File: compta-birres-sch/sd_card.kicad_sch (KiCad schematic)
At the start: 1 part, among them J1 SD_Card_Receptacle

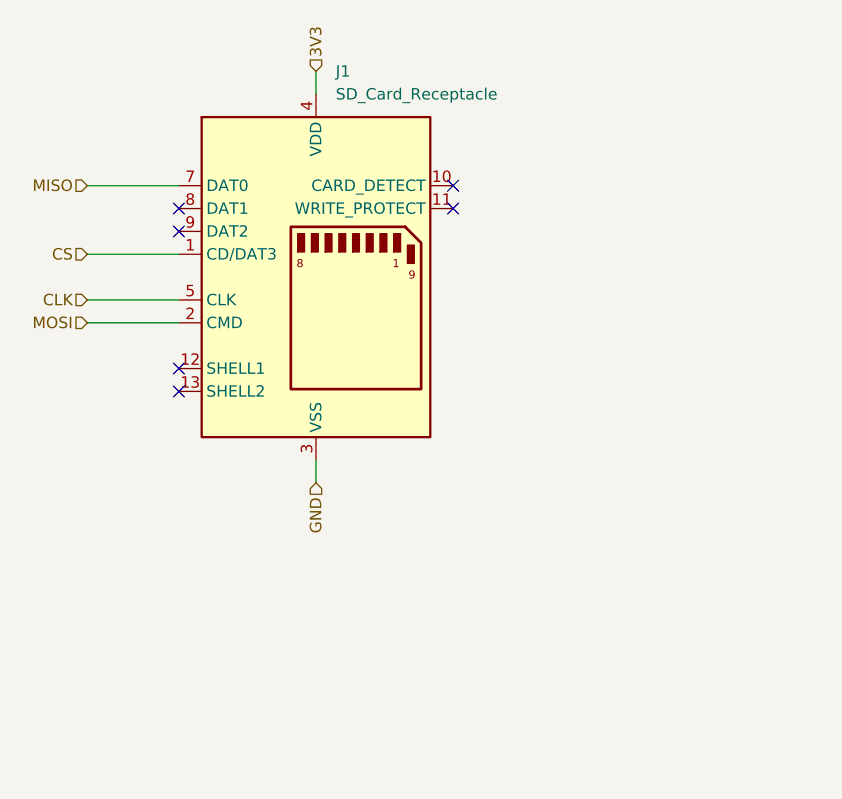
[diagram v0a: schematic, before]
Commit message: Schematics: Updated the display schematics
Now we no longer have the simple 0.56" 7 Segment display, we've built
custom displays with led strips.
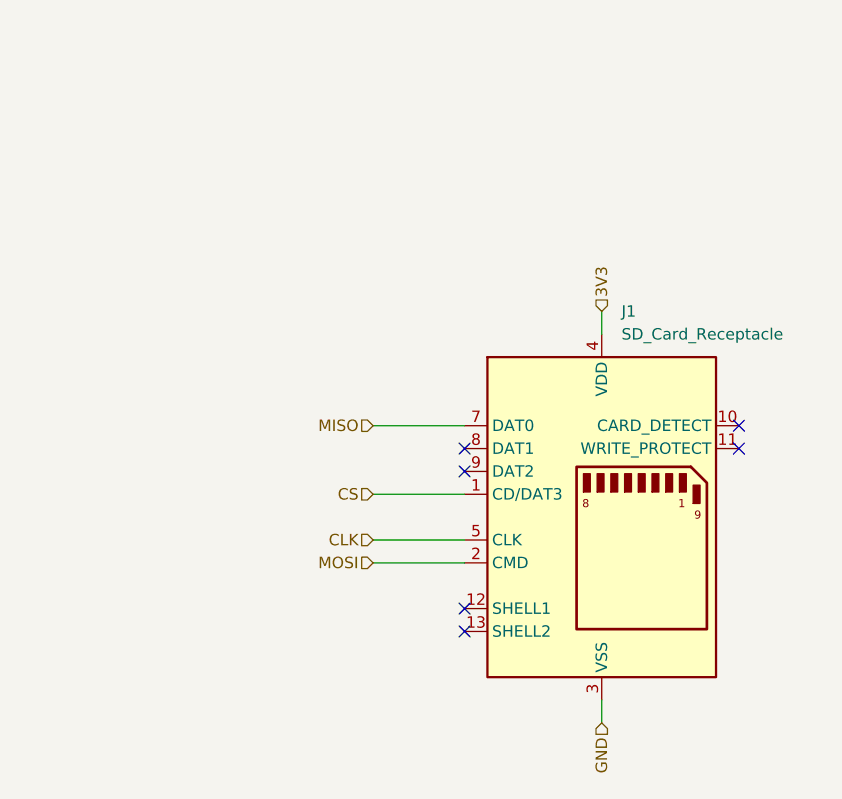
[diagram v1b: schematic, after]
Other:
- moved on the sheet: J1
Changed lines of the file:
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@@
 	(title_block
 		(title "SD Card")
-		(date "2024-08-01")
-		(rev "1.0")
+		(date "2024-08-08")
+		(rev "1.1")
 		(company "Associació Cultural TGK")
 	)
 	(no_connect
-		(at 99.06 63.5)
+		(at 130.81 90.17)
 	)
 	(no_connect
-		(at 129.54 60.96)
+		(at 161.29 87.63)
 	)
 	(no_connect
-		(at 99.06 78.74)
+		(at 130.81 105.41)
 	)
 	(no_connect
-		(at 99.06 81.28)
+		(at 130.81 107.95)
 	)
 	(no_connect
-		(at 99.06 60.96)
+		(at 130.81 87.63)
 	)
 	(no_connect
-		(at 129.54 58.42)
+		(at 161.29 85.09)
 	)
 	(wire
 		(pts
-			(xy 88.9 71.12) (xy 99.06 71.12)
+			(xy 120.65 97.79) (xy 130.81 97.79)
 		)
 		(stroke
@@
 	(wire
 		(pts
-			(xy 114.3 45.72) (xy 114.3 48.26)
+			(xy 146.05 72.39) (xy 146.05 74.93)
 		)
 		(stroke
@@
 	(wire
 		(pts
-			(xy 88.9 66.04) (xy 99.06 66.04)
+			(xy 120.65 92.71) (xy 130.81 92.71)
 		)
 		(stroke
@@
 	(wire
 		(pts
-			(xy 114.3 88.9) (xy 114.3 91.44)
+			(xy 146.05 115.57) (xy 146.05 118.11)
 		)
 		(stroke
@@
 	(wire
 		(pts
-			(xy 88.9 73.66) (xy 99.06 73.66)
+			(xy 120.65 100.33) (xy 130.81 100.33)
 		)
 		(stroke
@@
 	(wire
 		(pts
-			(xy 88.9 58.42) (xy 99.06 58.42)
+			(xy 120.65 85.09) (xy 130.81 85.09)
 		)
 		(stroke
@@
 	(hierarchical_label "3V3"
 		(shape input)
-		(at 114.3 45.72 90)
+		(at 146.05 72.39 90)
 		(fields_autoplaced yes)
 		(effects
@@
 	(hierarchical_label "MOSI"
 		(shape input)
-		(at 88.9 73.66 180)
+		(at 120.65 100.33 180)
 		(fields_autoplaced yes)
 		(effects
@@
 	(hierarchical_label "CS"
 		(shape input)
-		(at 88.9 66.04 180)
+		(at 120.65 92.71 180)
 		(fields_autoplaced yes)
 		(effects
@@
 	(hierarchical_label "GND"
 		(shape input)
-		(at 114.3 91.44 270)
+		(at 146.05 118.11 270)
 		(fields_autoplaced yes)
 		(effects
@@
 	(hierarchical_label "MISO"
 		(shape input)
-		(at 88.9 58.42 180)
+		(at 120.65 85.09 180)
 		(fields_autoplaced yes)
 		(effects
@@
 	(hierarchical_label "CLK"
 		(shape input)
-		(at 88.9 71.12 180)
+		(at 120.65 97.79 180)
 		(fields_autoplaced yes)
 		(effects
@@
 	(symbol
 		(lib_id "Connector:SD_Card_Receptacle")
-		(at 114.3 68.58 0)
+		(at 146.05 95.25 0)
 		(unit 1)
 		(exclude_from_sim no)
@@
 		(fields_autoplaced yes)
 		(property "Reference" "J1"
-			(at 116.4941 45.72 0)
+			(at 148.2441 72.39 0)
 			(effects
 				(font
@@
 		)
 		(property "Value" "SD_Card_Receptacle"
-			(at 116.4941 48.26 0)
+			(at 148.2441 74.93 0)
 			(effects
 				(font
@@
 		)
 		(property "Footprint" ""
-			(at 123.19 71.882 0)
+			(at 154.94 98.552 0)
 			(effects
 				(font
@@
 		)
 		(property "Datasheet" "http://portal.fciconnect.com/Comergent//fci/drawing/10067847.pdf"
-			(at 114.3 68.58 0)
+			(at 146.05 95.25 0)
 			(effects
 				(font
@@
 		)
 		(property "Description" "SD card receptacle"
-			(at 114.3 68.58 0)
+			(at 146.05 95.25 0)
 			(effects
 				(font
